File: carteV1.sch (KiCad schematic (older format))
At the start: 48 parts, among them CON1 USB-MINI-B, J12 FILTER_IOUT_DUT2, J6 REF_CLK_DUT2, J7 CRYSTAL OUTDUT2, T4 BALUN, T8 T1-1T, U1 AD9954, U2 LM1117MP-3.3, U5 MCP2210-SO, X1 25mhz

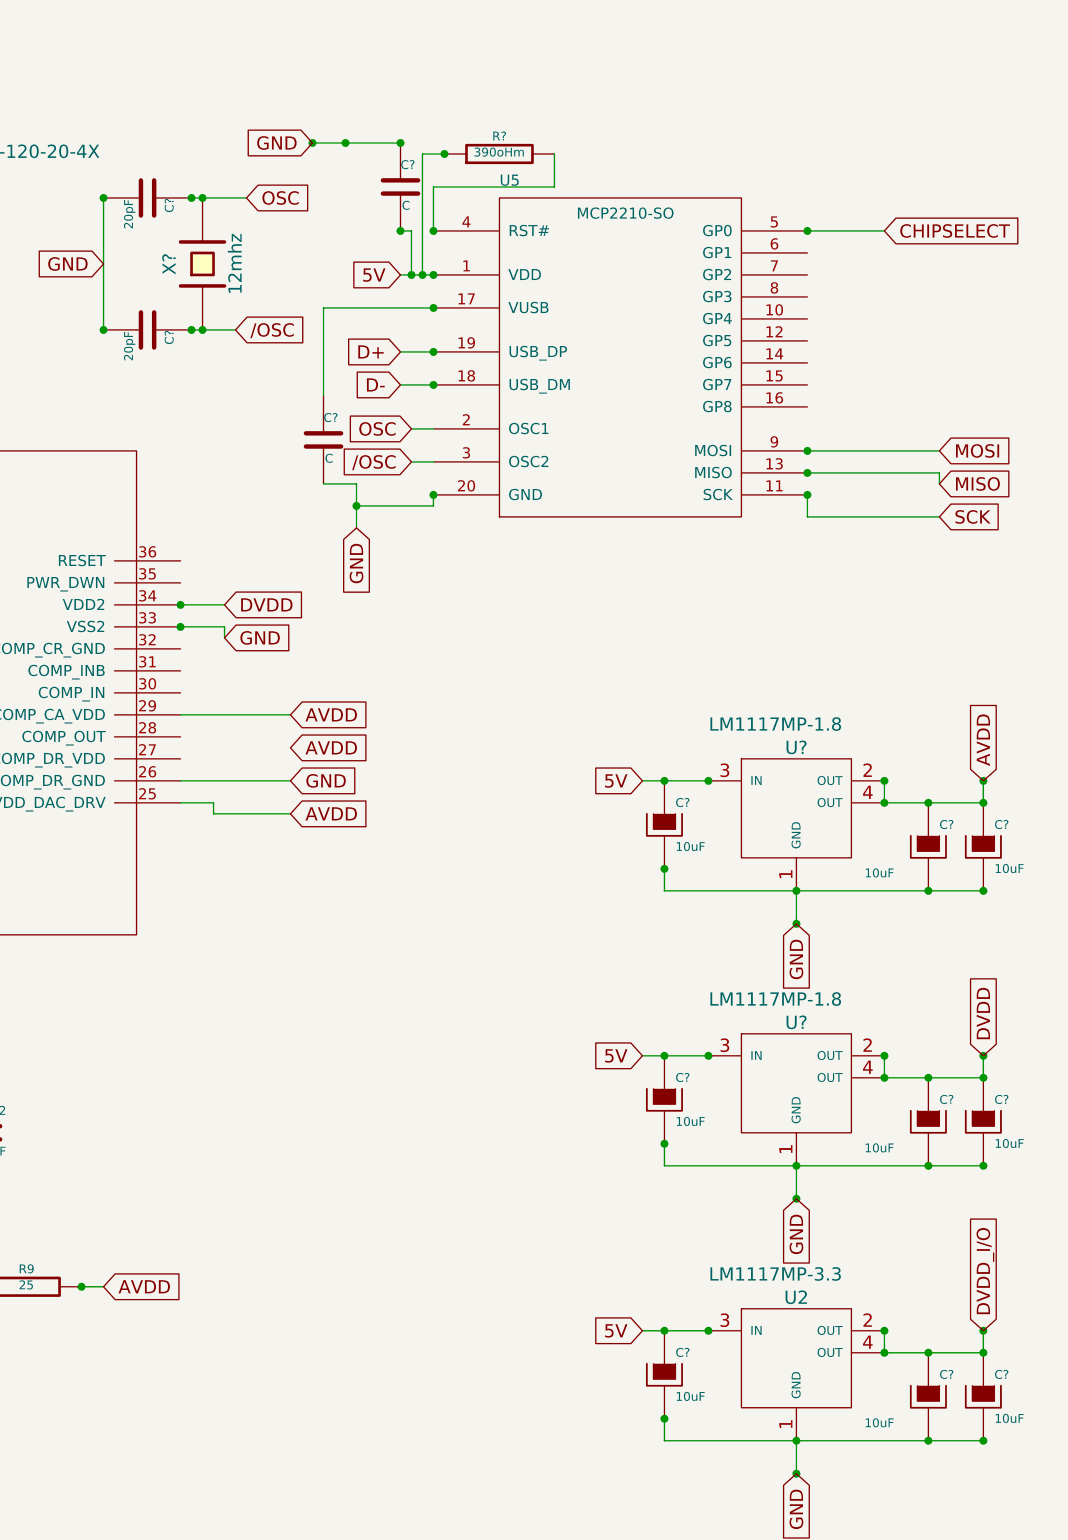
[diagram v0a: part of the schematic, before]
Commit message: Numérotation des composants
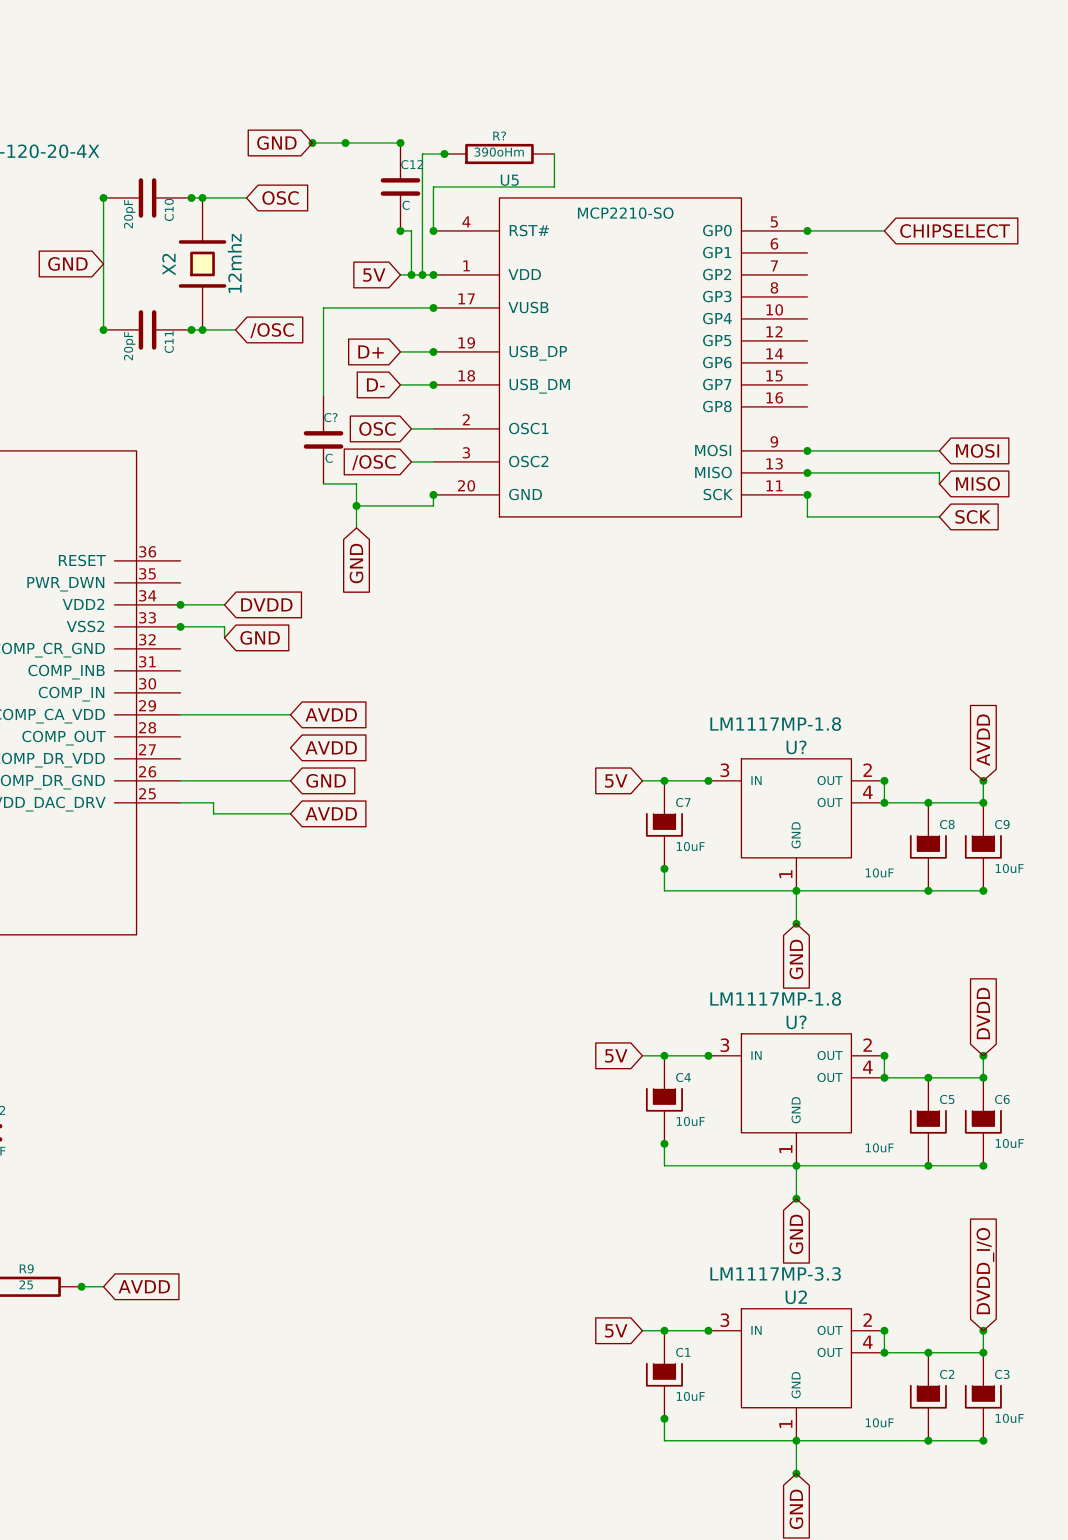
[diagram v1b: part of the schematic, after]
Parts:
- gave numbers to parts that had none: 13
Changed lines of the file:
@@
 Sheet 1 1
 Title "AD9954 - GENERATION SIGNAL HF"
-Date "21 may 2014"
+Date "22 may 2014"
 Rev "0.1"
 Comp "Polytech'Tours"
@@
 GND
 $Comp
-L CAPAPOL C?
+L CAPAPOL C1
 U 1 1 537A99AC
 P 9400 6200
-F 0 "C?" H 9450 6300 40  0000 L CNN
+F 0 "C1" H 9450 6300 40  0000 L CNN
 F 1 "10uF" H 9450 6100 40  0000 L CNN
 F 2 "~" H 9500 6050 30  0000 C CNN
@@
 $EndComp
 $Comp
-L CAPAPOL C?
+L CAPAPOL C3
 U 1 1 537A99B9
 P 10850 6300
-F 0 "C?" H 10900 6400 40  0000 L CNN
+F 0 "C3" H 10900 6400 40  0000 L CNN
 F 1 "10uF" H 10900 6200 40  0000 L CNN
 F 2 "~" H 10950 6150 30  0000 C CNN
@@
 $EndComp
 $Comp
-L CAPAPOL C?
+L CAPAPOL C2
 U 1 1 537A99C9
 P 10600 6300
-F 0 "C?" H 10650 6400 40  0000 L CNN
+F 0 "C2" H 10650 6400 40  0000 L CNN
 F 1 "10uF" H 10309 6180 40  0000 L CNN
 F 2 "~" H 10700 6150 30  0000 C CNN
@@
 GND
 $Comp
-L CRYSTAL X?
+L CRYSTAL X2
 U 1 1 537AA364
 P 7300 1150
-F 0 "X?" H 7300 1300 60  0000 C CNN
+F 0 "X2" H 7300 1300 60  0000 C CNN
 F 1 "12mhz" H 7300 1000 60  0000 C CNN
 F 2 "~" H 7300 1150 60  0000 C CNN
@@
 $EndComp
 $Comp
-L C C?
+L C C10
 U 1 1 537AA36A
 P 7050 850
-F 0 "C?" H 7050 950 40  0000 L CNN
+F 0 "C10" H 7050 950 40  0000 L CNN
 F 1 "20pF" H 7056 765 40  0000 L CNN
 F 2 "~" H 7088 700 30  0000 C CNN
@@
 $EndComp
 $Comp
-L C C?
+L C C11
 U 1 1 537AA370
 P 7050 1450
-F 0 "C?" H 7050 1550 40  0000 L CNN
+F 0 "C11" H 7050 1550 40  0000 L CNN
 F 1 "20pF" H 7056 1365 40  0000 L CNN
 F 2 "~" H 7088 1300 30  0000 C CNN
@@
 5V
 $Comp
-L C C?
+L C C12
 U 1 1 537AD1AA
 P 8200 800
-F 0 "C?" H 8200 900 40  0000 L CNN
+F 0 "C12" H 8200 900 40  0000 L CNN
 F 1 "C" H 8206 715 40  0000 L CNN
 F 2 "~" H 8238 650 30  0000 C CNN
@@
 GND
 $Comp
-L CAPAPOL C?
+L CAPAPOL C4
 U 1 1 537BAB16
 P 9400 4950
-F 0 "C?" H 9450 5050 40  0000 L CNN
+F 0 "C4" H 9450 5050 40  0000 L CNN
 F 1 "10uF" H 9450 4850 40  0000 L CNN
 F 2 "~" H 9500 4800 30  0000 C CNN
@@
 $EndComp
 $Comp
-L CAPAPOL C?
+L CAPAPOL C6
 U 1 1 537BAB1C
 P 10850 5050
-F 0 "C?" H 10900 5150 40  0000 L CNN
+F 0 "C6" H 10900 5150 40  0000 L CNN
 F 1 "10uF" H 10900 4950 40  0000 L CNN
 F 2 "~" H 10950 4900 30  0000 C CNN
@@
 $EndComp
 $Comp
-L CAPAPOL C?
+L CAPAPOL C5
 U 1 1 537BAB22
 P 10600 5050
-F 0 "C?" H 10650 5150 40  0000 L CNN
+F 0 "C5" H 10650 5150 40  0000 L CNN
 F 1 "10uF" H 10309 4930 40  0000 L CNN
 F 2 "~" H 10700 4900 30  0000 C CNN
@@
 GND
 $Comp
-L CAPAPOL C?
+L CAPAPOL C7
 U 1 1 537BAB51
 P 9400 3700
-F 0 "C?" H 9450 3800 40  0000 L CNN
+F 0 "C7" H 9450 3800 40  0000 L CNN
 F 1 "10uF" H 9450 3600 40  0000 L CNN
 F 2 "~" H 9500 3550 30  0000 C CNN
@@
 $EndComp
 $Comp
-L CAPAPOL C?
+L CAPAPOL C9
 U 1 1 537BAB57
 P 10850 3800
-F 0 "C?" H 10900 3900 40  0000 L CNN
+F 0 "C9" H 10900 3900 40  0000 L CNN
 F 1 "10uF" H 10900 3700 40  0000 L CNN
 F 2 "~" H 10950 3650 30  0000 C CNN
@@
 $EndComp
 $Comp
-L CAPAPOL C?
+L CAPAPOL C8
 U 1 1 537BAB5D
 P 10600 3800
-F 0 "C?" H 10650 3900 40  0000 L CNN
+F 0 "C8" H 10650 3900 40  0000 L CNN
 F 1 "10uF" H 10309 3680 40  0000 L CNN
 F 2 "~" H 10700 3650 30  0000 C CNN

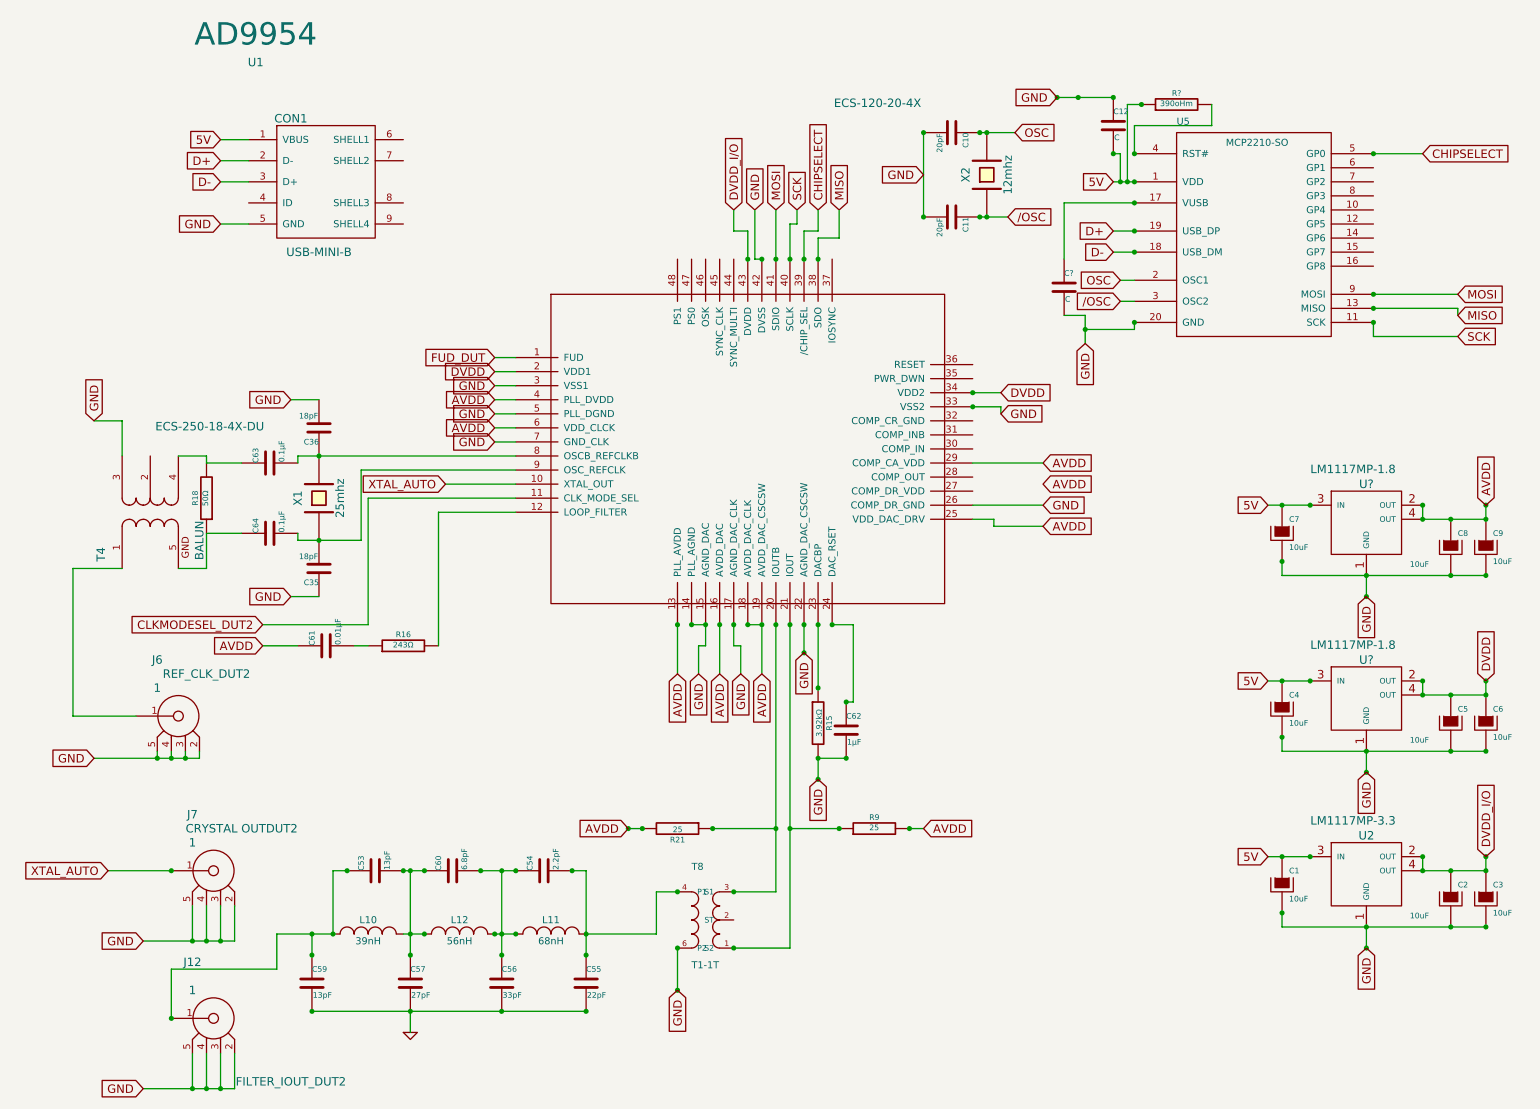
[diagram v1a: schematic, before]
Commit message: Ajout des footprints et liaisons
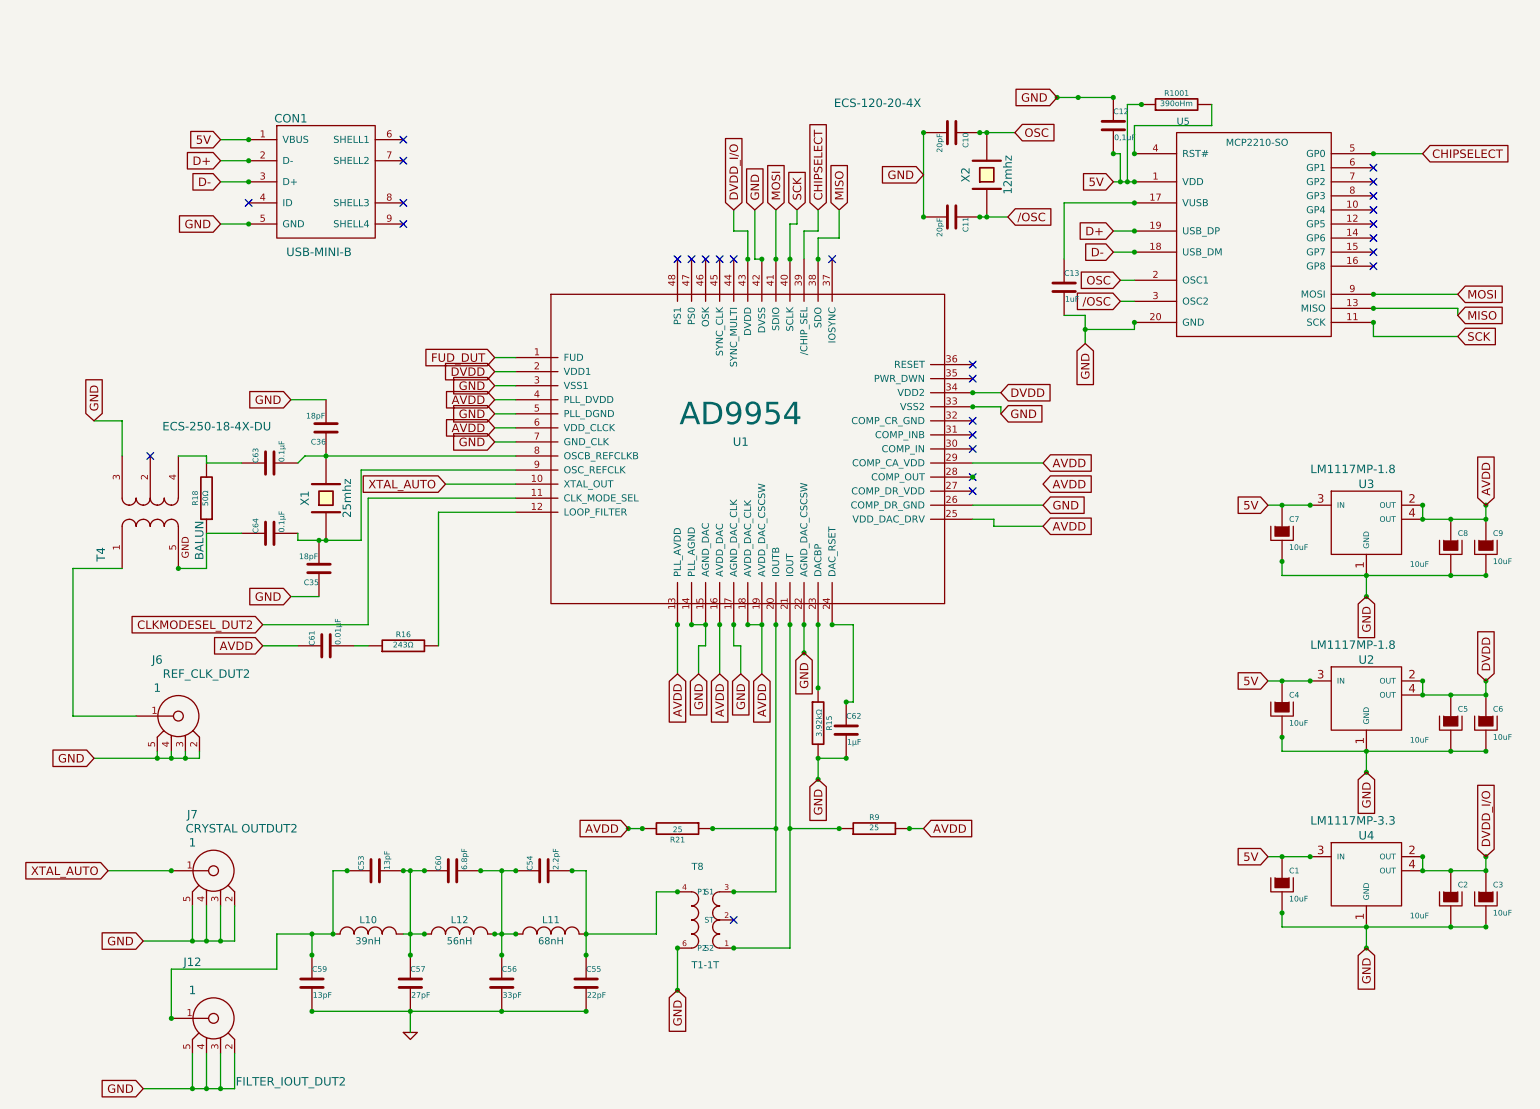
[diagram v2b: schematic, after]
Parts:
- C12: value C -> 0,1uF
- C13: renamed from C?; value C -> 1uF; footprint ~ -> (none)
- gave numbers to parts that had none: 3
- renumbered U2 to U4
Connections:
- no-connect marks 0 -> 28
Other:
- moved on the sheet: C36, X1
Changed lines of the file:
@@
 L CRYSTAL X1
 U 1 1 537A0ADF
-P 2550 3450
-F 0 "X1" H 2550 3600 60  0000 C CNN
-F 1 "25mhz" H 2550 3300 60  0000 C CNN
-F 2 "~" H 2550 3450 60  0000 C CNN
-F 3 "ECS-250-18-4X-DU" V 3060 4227 60  0000 C CNN
-	1    2550 3450
+P 2600 3450
+F 0 "X1" H 2600 3600 60  0000 C CNN
+F 1 "25mhz" H 2600 3300 60  0000 C CNN
+F 2 "~" H 2600 3450 60  0000 C CNN
+F 3 "ECS-250-18-4X-DU" V 3110 4227 60  0000 C CNN
+	1    2600 3450
 	0    -1   -1   0
 $EndComp
@@
 L C C36
 U 1 1 537A0D25
-P 2550 2950
-F 0 "C36" H 2550 3050 40  0000 L CNN
-F 1 "18pF" H 2556 2865 40  0000 L CNN
-F 2 "~" H 2588 2800 30  0000 C CNN
-F 3 "" H 2550 2950 60  0000 C CNN
-	1    2550 2950
+P 2600 2950
+F 0 "C36" H 2600 3050 40  0000 L CNN
+F 1 "18pF" H 2606 2865 40  0000 L CNN
+F 2 "~" H 2638 2800 30  0000 C CNN
+F 3 "" H 2600 2950 60  0000 C CNN
+	1    2600 2950
 	-1   0    0    1
 $EndComp
@@
 $EndComp
 $Comp
-L LM1117MP-3.3 U2
+L LM1117MP-3.3 U4
 U 1 1 537A8393
 P 10000 6150
-F 0 "U2" H 10000 6450 60  0000 C CNN
+F 0 "U4" H 10000 6450 60  0000 C CNN
 F 1 "LM1117MP-3.3" H 9601 6556 60  0000 L CNN
 F 2 "" H 10000 6150 60  0000 C CNN
@@
 P 8200 800
 F 0 "C12" H 8200 900 40  0000 L CNN
-F 1 "C" H 8206 715 40  0000 L CNN
+F 1 "0,1uF" H 8206 715 40  0000 L CNN
 F 2 "~" H 8238 650 30  0000 C CNN
 F 3 "~" H 8200 800 60  0000 C CNN
@@
 $EndComp
 $Comp
-L C C?
+L C C13
 U 1 1 537AD513
 P 7850 1950
-F 0 "C?" H 7850 2050 40  0000 L CNN
-F 1 "C" H 7856 1865 40  0000 L CNN
-F 2 "~" H 7888 1800 30  0000 C CNN
+F 0 "C13" H 7850 2050 40  0000 L CNN
+F 1 "1uF" H 7856 1865 40  0000 L CNN
+F 2 "" H 7888 1800 30  0000 C CNN
 F 3 "~" H 7850 1950 60  0000 C CNN
 	1    7850 1950
@@
 $EndComp
 $Comp
-L LM1117MP-3.3 U?
+L LM1117MP-3.3 U2
 U 1 1 537BAB0D
 P 10000 4900
-F 0 "U?" H 10000 5200 60  0000 C CNN
+F 0 "U2" H 10000 5200 60  0000 C CNN
 F 1 "LM1117MP-1.8" H 9601 5306 60  0000 L CNN
 F 2 "" H 10000 4900 60  0000 C CNN
@@
 $EndComp
 $Comp
-L LM1117MP-3.3 U?
+L LM1117MP-3.3 U3
 U 1 1 537BAB48
 P 10000 3650
-F 0 "U?" H 10000 3950 60  0000 C CNN
+F 0 "U3" H 10000 3950 60  0000 C CNN
 F 1 "LM1117MP-1.8" H 9601 4056 60  0000 L CNN
 F 2 "" H 10000 3650 60  0000 C CNN
@@
 GND
 $Comp
-L R R?
+L R R1001
 U 1 1 537BC0C4
 P 8650 650
-F 0 "R?" V 8730 650 40  0000 C CNN
+F 0 "R1001" V 8730 650 40  0000 C CNN
 F 1 "390oHm" V 8657 651 40  0000 C CNN
 F 2 "~" V 8580 650 30  0000 C CNN
@@
 Text GLabel 7450 1450 2    60   Input ~ 0
 /OSC
-$Comp
-L AD9954 U1
-U 1 1 537A9C40
-P 5550 3050
-F 0 "U1" H 2100 5750 60  0000 C CNN
-F 1 "AD9954" H 2100 5950 159 0000 C CNN
-F 2 "~" H 2100 5950 60  0000 C CNN
-F 3 "~" H 2100 5950 60  0000 C CNN
-	1    5550 3050
-	1    0    0    -1
-$EndComp
+NoConn ~ 7200 2500
+NoConn ~ 7200 2600
+NoConn ~ 7200 2900
+NoConn ~ 7200 3000
+NoConn ~ 7200 3100
+NoConn ~ 5100 1750
+NoConn ~ 5200 1750
+NoConn ~ 5300 1750
+NoConn ~ 5400 1750
+NoConn ~ 5500 1750
+NoConn ~ 6200 1750
+NoConn ~ 7200 3300
+NoConn ~ 7200 3400
+NoConn ~ 10050 1100
+NoConn ~ 10050 1200
+NoConn ~ 10050 1300
+NoConn ~ 10050 1400
+NoConn ~ 10050 1500
+NoConn ~ 10050 1600
+NoConn ~ 10050 1700
+NoConn ~ 10050 1800
+NoConn ~ 3150 900
+NoConn ~ 3150 1050
+NoConn ~ 3150 1350
+NoConn ~ 3150 1500
+NoConn ~ 2050 1350
 Wire Wire Line
 	8250 2050 8350 2050
@@
 	9400 4000 9400 3900
 Wire Wire Line
-	10850 4000 9400 4000
+	9400 4000 10850 4000
 Connection ~ 9600 3500
 Connection ~ 9400 3500
 Wire Wire Line
-	9600 3500 9300 3500
+	9300 3500 9600 3500
 Connection ~ 10850 4750
 Wire Wire Line
@@
 	9400 5250 9400 5150
 Wire Wire Line
-	10850 5250 9400 5250
+	9400 5250 10850 5250
 Connection ~ 9600 4750
 Connection ~ 9400 4750
 Wire Wire Line
-	9600 4750 9300 4750
+	9300 4750 9600 4750
 Connection ~ 10850 6000
 Wire Wire Line
@@
 	9400 6500 9400 6400
 Wire Wire Line
-	10850 6500 9400 6500
+	9400 6500 10850 6500
 Connection ~ 9600 6000
 Connection ~ 9400 6000
 Wire Wire Line
-	9600 6000 9300 6000
+	9300 6000 9600 6000
 Connection ~ 5100 6650
 Connection ~ 5100 6950
@@
 Connection ~ 5800 1750
 Connection ~ 5900 1750
-Connection ~ 6000 1750
 Connection ~ 6100 1750
 Wire Wire Line
@@
 Connection ~ 5500 4350
 Wire Wire Line
-	3800 2450 3950 2450
-Wire Wire Line
 	3800 2550 3950 2550
 Wire Wire Line
@@
 	1750 3200 2000 3200
 Wire Wire Line
-	2400 3200 2400 3150
-Wire Wire Line
-	2400 3150 3950 3150
+	2400 3200 2450 3150
+Wire Wire Line
+	2450 3150 3950 3150
 Wire Wire Line
 	2400 3700 2400 3750
 Wire Wire Line
 	2400 3750 2850 3750
-Connection ~ 2550 3150
+Connection ~ 2600 3150
 Wire Wire Line
 	2850 3750 2850 3250
@@
 	1850 1050 2050 1050
 Wire Wire Line
+	2350 2750 2600 2750
+Connection ~ 7200 3300
+Wire Wire Line
 	1850 900  2050 900
-Wire Wire Line
-	2350 2750 2550 2750
+Connection ~ 2050 900
+Connection ~ 2050 1050
+Connection ~ 2050 1200
+Connection ~ 2050 1500
+NoConn ~ 5500 6450
+$Comp
+L AD9954 U1
+U 1 1 537DEC5D
+P 5550 3050
+F 0 "U1" H 5550 3050 60  0000 C CNN
+F 1 "AD9954" H 5550 3250 159 0000 C CNN
+F 2 "~" H 5550 3250 60  0000 C CNN
+F 3 "~" H 5550 3250 60  0000 C CNN
+	1    5550 3050
+	1    0    0    -1
+$EndComp
+Connection ~ 2600 3750
+Connection ~ 1550 3950
+NoConn ~ 1350 3150
+Wire Wire Line
+	3800 2450 3950 2450
 $EndSCHEMATC
